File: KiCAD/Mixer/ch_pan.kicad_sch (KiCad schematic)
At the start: 3 parts

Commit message: Power Bus, Footprints, Audio Bus
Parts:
- R10, R9: footprint (none) -> Resistor_SMD:R_0805_2012Metric_Pad1.20x1.40mm_HandSolder
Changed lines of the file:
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@@
 			)
 		)
-		(property "Footprint" ""
+		(property "Footprint" "Resistor_SMD:R_0805_2012Metric_Pad1.20x1.40mm_HandSolder"
 			(at 58.42 51.308 90)
 			(hide yes)
@@
 			)
 		)
-		(property "Footprint" ""
+		(property "Footprint" "Resistor_SMD:R_0805_2012Metric_Pad1.20x1.40mm_HandSolder"
 			(at 58.42 56.388 90)
 			(hide yes)

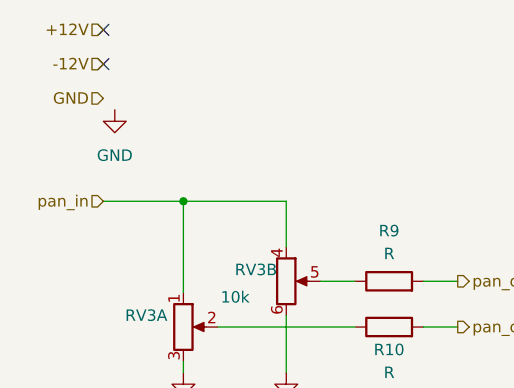
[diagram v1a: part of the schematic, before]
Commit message: added second channel and footprints / created PCB desing...might make PCB bit bigger
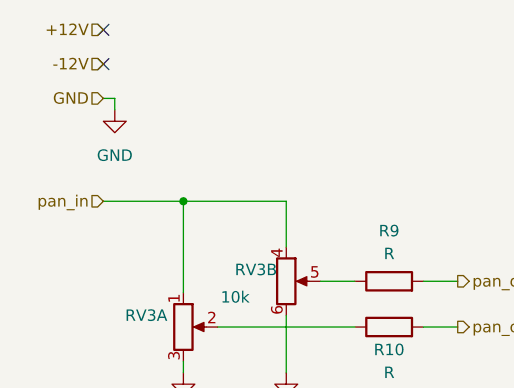
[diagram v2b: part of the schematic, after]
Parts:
- RV3: footprint (none) -> Potentiometer_THT:Potentiometer_Alps_RK09L_Double_Vertical
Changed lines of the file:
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@@
+	(wire
+		(pts
+			(xy 27.94 30.48) (xy 27.94 29.21)
+		)
+		(stroke
+			(width 0)
+			(type default)
+		)
+	)
 	(wire
 		(pts
@@
 		(pts
 			(xy 46.99 45.72) (xy 46.99 40.64)
+		)
+		(stroke
+			(width 0)
+			(type default)
+		)
+	)
+	(wire
+		(pts
+			(xy 26.67 29.21) (xy 27.94 29.21)
 		)
 		(stroke
@@
 			)
 		)
-		(property "Footprint" ""
+		(property "Footprint" "Potentiometer_THT:Potentiometer_Alps_RK09L_Double_Vertical"
 			(at 35.56 54.61 0)
 			(hide yes)
@@
 				(path "/322d427a-6aae-4762-92d6-d97688daf29b/8a2849b7-184d-4014-bb98-da9dec8b5f90/c0c3c81f-4e29-495b-ab2b-e1d97e6e442d"
 					(reference "RV3")
+					(unit 1)
+				)
+				(path "/322d427a-6aae-4762-92d6-d97688daf29b/8a2849b7-184d-4014-bb98-da9dec8b5f90/cea36016-c788-4767-8a0d-1508f3be4f70"
+					(reference "RV7")
 					(unit 1)
 				)
@@
 			)
 		)
-		(property "Footprint" ""
+		(property "Footprint" "Potentiometer_THT:Potentiometer_Alps_RK09L_Double_Vertical"
 			(at 46.99 49.53 0)
 			(hide yes)
@@
 				(path "/322d427a-6aae-4762-92d6-d97688daf29b/8a2849b7-184d-4014-bb98-da9dec8b5f90/c0c3c81f-4e29-495b-ab2b-e1d97e6e442d"
 					(reference "RV3")
+					(unit 2)
+				)
+				(path "/322d427a-6aae-4762-92d6-d97688daf29b/8a2849b7-184d-4014-bb98-da9dec8b5f90/cea36016-c788-4767-8a0d-1508f3be4f70"
+					(reference "RV7")
 					(unit 2)
 				)
@@
 					(unit 1)
 				)
+				(path "/322d427a-6aae-4762-92d6-d97688daf29b/8a2849b7-184d-4014-bb98-da9dec8b5f90/cea36016-c788-4767-8a0d-1508f3be4f70"
+					(reference "#PWR090")
+					(unit 1)
+				)
 			)
 		)
@@
 				(path "/322d427a-6aae-4762-92d6-d97688daf29b/8a2849b7-184d-4014-bb98-da9dec8b5f90/c0c3c81f-4e29-495b-ab2b-e1d97e6e442d"
 					(reference "R9")
+					(unit 1)
+				)
+				(path "/322d427a-6aae-4762-92d6-d97688daf29b/8a2849b7-184d-4014-bb98-da9dec8b5f90/cea36016-c788-4767-8a0d-1508f3be4f70"
+					(reference "R21")
 					(unit 1)
 				)
@@
 					(unit 1)
 				)
+				(path "/322d427a-6aae-4762-92d6-d97688daf29b/8a2849b7-184d-4014-bb98-da9dec8b5f90/cea36016-c788-4767-8a0d-1508f3be4f70"
+					(reference "#PWR091")
+					(unit 1)
+				)
 			)
 		)
@@
 					(unit 1)
 				)
+				(path "/322d427a-6aae-4762-92d6-d97688daf29b/8a2849b7-184d-4014-bb98-da9dec8b5f90/cea36016-c788-4767-8a0d-1508f3be4f70"
+					(reference "#PWR092")
+					(unit 1)
+				)
 			)
 		)
@@
 					(unit 1)
 				)
+				(path "/322d427a-6aae-4762-92d6-d97688daf29b/8a2849b7-184d-4014-bb98-da9dec8b5f90/cea36016-c788-4767-8a0d-1508f3be4f70"
+					(reference "R22")
+					(unit 1)
+				)

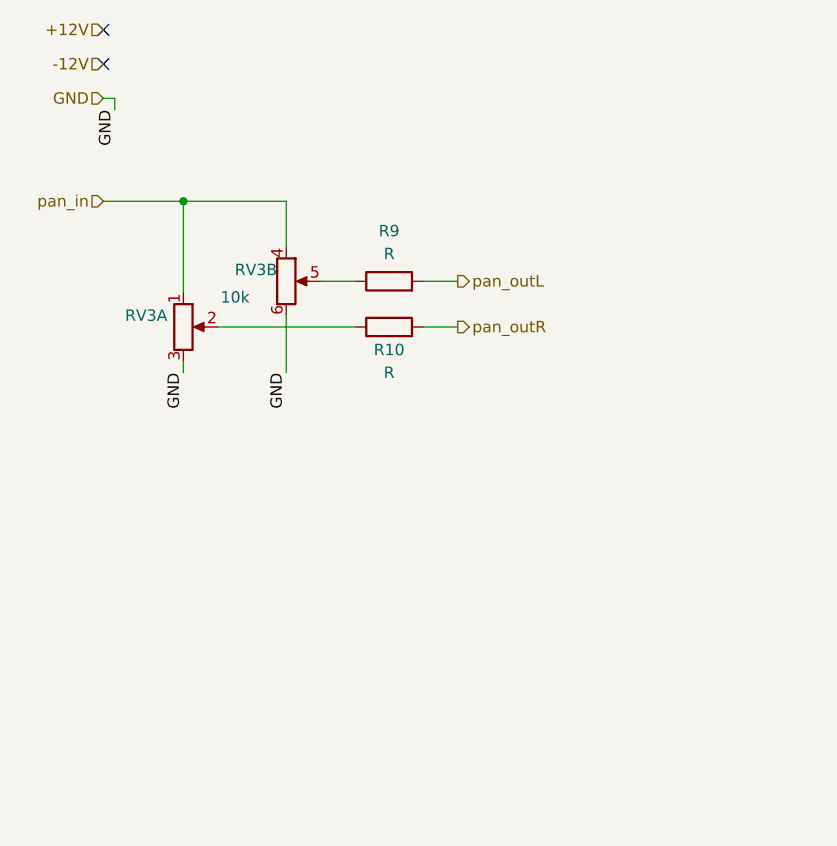
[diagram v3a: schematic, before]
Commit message: Rework of schematic, with error fixes and reworked pcb
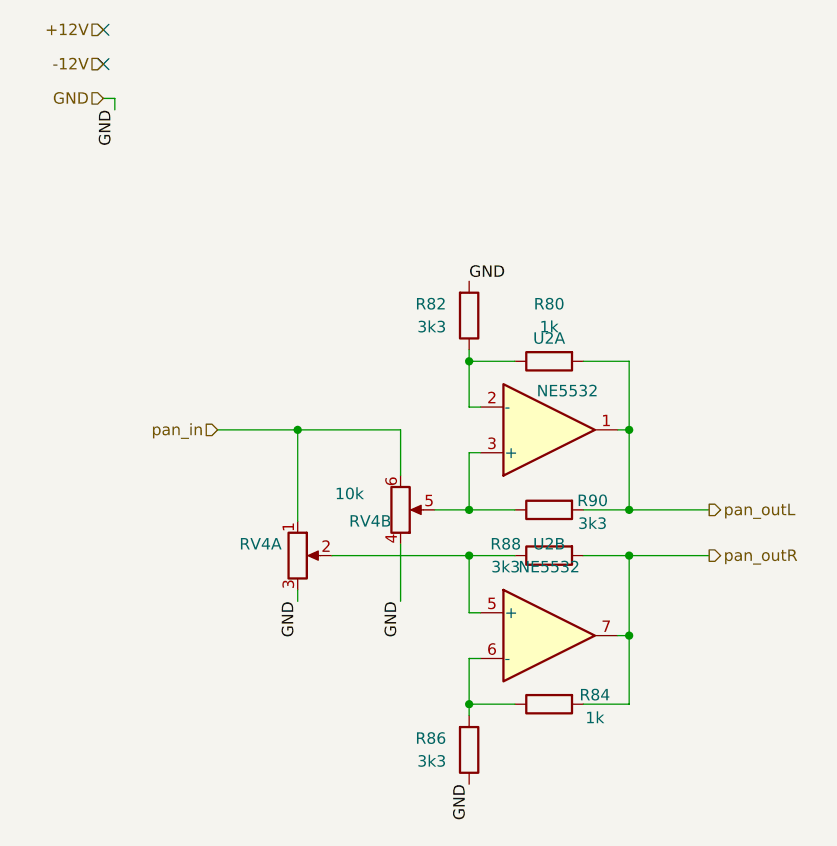
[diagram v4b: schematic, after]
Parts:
- removed R10, R9: R, Resistor_SMD:R_0805_2012Metric_Pad1.20x1.40mm_HandSolder, symbol Device:R
- added R80, R84: 1k, Resistor_SMD:R_0805_2012Metric_Pad1.20x1.40mm_HandSolder, symbol Device:R
- added R82, R86, R88, R90: 3k3, Resistor_SMD:R_0805_2012Metric_Pad1.20x1.40mm_HandSolder, symbol Device:R
- added U2: NE5532, Package_SO:SOIC-8_3.9x4.9mm_P1.27mm, symbol Amplifier_Operational:NE5532
- renumbered RV3 to RV4
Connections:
- net GND: now also RV4.4, R82.2, R86.1; no longer RV4.6
- net pan_in: now also RV4.6; no longer RV4.4
- net pan_outL: now also R80.2, R90.2, U2.1
- net pan_outR: now also R84.2, R88.2, U2.7
- net at RV4.2: now also R88.1, U2.5 (+)
- net at RV4.5: now also R90.1, U2.3 (+)
- new net: R80.1, R82.1, U2.2 (-)
- new net: R84.1, R86.2, U2.6 (-)
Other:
- moved on the sheet: RV4A, RV4B

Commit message: Final PCB Version that got ordered from JLCPCB
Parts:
- renumbered R82 to R15, R86 to R16, R80 to R17, R90 to R18, R88 to R19, R84 to R20, RV4 to RV3, U2 to U3
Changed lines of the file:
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@@
 		(in_pos_files yes)
 		(dnp no)
-		(property "Reference" "RV4"
+		(property "Reference" "RV3"
 			(at 46.482 78.74 0)
 			(show_name no)
@@
 			(project "Mixer"
 				(path "/322d427a-6aae-4762-92d6-d97688daf29b/8a2849b7-184d-4014-bb98-da9dec8b5f90/c0c3c81f-4e29-495b-ab2b-e1d97e6e442d"
-					(reference "RV4")
+					(reference "RV3")
 					(unit 1)
 				)
@@
 		(dnp no)
 		(fields_autoplaced yes)
-		(property "Reference" "R82"
+		(property "Reference" "R15"
 			(at 64.77 52.07 0)
 			(show_name no)
@@
 			(project "Mixer"
 				(path "/322d427a-6aae-4762-92d6-d97688daf29b/8a2849b7-184d-4014-bb98-da9dec8b5f90/c0c3c81f-4e29-495b-ab2b-e1d97e6e442d"
-					(reference "R82")
+					(reference "R15")
 					(unit 1)
 				)
@@
 		(in_pos_files yes)
 		(dnp no)
-		(property "Reference" "R90"
+		(property "Reference" "R18"
 			(at 81.026 73.914 90)
 			(show_name no)
@@
 			(project "Mixer"
 				(path "/322d427a-6aae-4762-92d6-d97688daf29b/8a2849b7-184d-4014-bb98-da9dec8b5f90/c0c3c81f-4e29-495b-ab2b-e1d97e6e442d"
-					(reference "R90")
+					(reference "R18")
 					(unit 1)
 				)
@@
 		(in_pos_files yes)
 		(dnp no)
-		(property "Reference" "RV4"
+		(property "Reference" "RV3"
 			(at 58.674 76.2 0)
 			(show_name no)
@@
 			(project "Mixer"
 				(path "/322d427a-6aae-4762-92d6-d97688daf29b/8a2849b7-184d-4014-bb98-da9dec8b5f90/c0c3c81f-4e29-495b-ab2b-e1d97e6e442d"
-					(reference "RV4")
+					(reference "RV3")
 					(unit 2)
 				)
@@
 		(in_pos_files yes)
 		(dnp no)
-		(property "Reference" "R88"
+		(property "Reference" "R19"
 			(at 71.374 78.74 90)
 			(show_name no)
@@
 			(project "Mixer"
 				(path "/322d427a-6aae-4762-92d6-d97688daf29b/8a2849b7-184d-4014-bb98-da9dec8b5f90/c0c3c81f-4e29-495b-ab2b-e1d97e6e442d"
-					(reference "R88")
+					(reference "R19")
 					(unit 1)
 				)
@@
 		(dnp no)
 		(fields_autoplaced yes)
-		(property "Reference" "U2"
+		(property "Reference" "U3"
 			(at 76.2 78.74 0)
 			(show_name no)
@@
 			(project "Mixer"
 				(path "/322d427a-6aae-4762-92d6-d97688daf29b/8a2849b7-184d-4014-bb98-da9dec8b5f90/c0c3c81f-4e29-495b-ab2b-e1d97e6e442d"
-					(reference "U2")
+					(reference "U3")
 					(unit 2)
 				)
@@
 		(dnp no)
 		(fields_autoplaced yes)
-		(property "Reference" "R80"
+		(property "Reference" "R17"
 			(at 76.2 52.07 90)
 			(show_name no)
@@
 			(project "Mixer"
 				(path "/322d427a-6aae-4762-92d6-d97688daf29b/8a2849b7-184d-4014-bb98-da9dec8b5f90/c0c3c81f-4e29-495b-ab2b-e1d97e6e442d"
-					(reference "R80")
+					(reference "R17")
 					(unit 1)
 				)
@@
 		(in_pos_files yes)
 		(dnp no)
-		(property "Reference" "R84"
+		(property "Reference" "R20"
 			(at 81.28 95.504 90)
 			(show_name no)
@@
 			(project "Mixer"
 				(path "/322d427a-6aae-4762-92d6-d97688daf29b/8a2849b7-184d-4014-bb98-da9dec8b5f90/c0c3c81f-4e29-495b-ab2b-e1d97e6e442d"
-					(reference "R84")
+					(reference "R20")
 					(unit 1)
 				)
@@
 		(dnp no)
 		(fields_autoplaced yes)
-		(property "Reference" "R86"
+		(property "Reference" "R16"
 			(at 64.77 100.33 0)
 			(show_name no)
@@
 			(project "Mixer"
 				(path "/322d427a-6aae-4762-92d6-d97688daf29b/8a2849b7-184d-4014-bb98-da9dec8b5f90/c0c3c81f-4e29-495b-ab2b-e1d97e6e442d"
-					(reference "R86")
+					(reference "R16")
 					(unit 1)
 				)
@@
 		(in_pos_files yes)
 		(dnp no)
-		(property "Reference" "U2"
+		(property "Reference" "U3"
 			(at 76.2 55.88 0)
 			(show_name no)
@@
 			(project "Mixer"
 				(path "/322d427a-6aae-4762-92d6-d97688daf29b/8a2849b7-184d-4014-bb98-da9dec8b5f90/c0c3c81f-4e29-495b-ab2b-e1d97e6e442d"
-					(reference "U2")
+					(reference "U3")
 					(unit 1)
 				)
